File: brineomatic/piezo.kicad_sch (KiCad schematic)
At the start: 4 parts, among them Q2 AO3400A

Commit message: added qwiic i2c connector
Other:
- title: (none) -> https://github.com/hoeken/brineomatic
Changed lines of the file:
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@@
 	(generator_version "9.0")
 	(paper "A4")
+	(title_block
+		(title "https://github.com/hoeken/brineomatic")
+		(date "2025-08-28")
+		(rev "B")
+	)
 	(rectangle
 		(start 110.49 58.42)

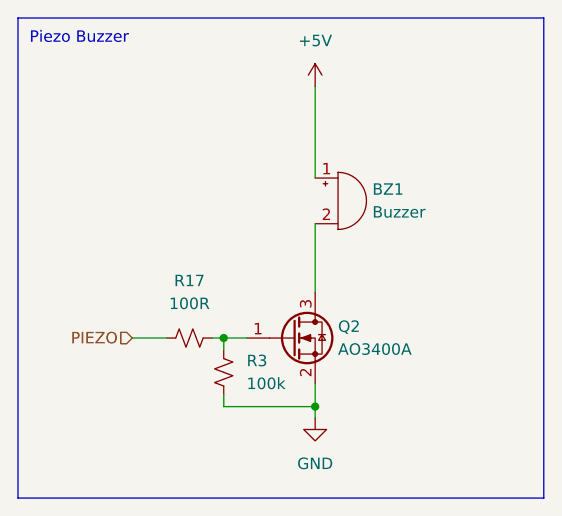
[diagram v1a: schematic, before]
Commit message: added pullup resistor to adc alert
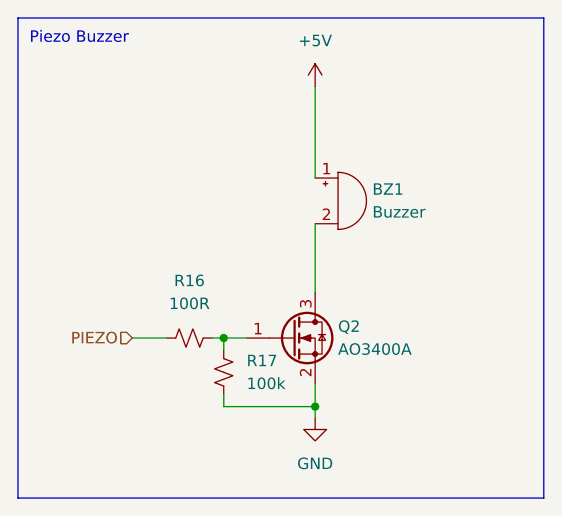
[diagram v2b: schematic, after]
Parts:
- renumbered R17 to R16, R3 to R17
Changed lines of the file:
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@@
 		(dnp no)
 		(fields_autoplaced yes)
-		(property "Reference" "#PWR023"
+		(property "Reference" "#PWR025"
 			(at 143.51 69.85 0)
 			(effects
@@
 			(project "brineomatic"
 				(path "/96477ae2-ef08-48f3-8dd4-fe4478541f68/d9651726-ebc8-4cdb-a521-a43a3039a77a"
-					(reference "#PWR023")
+					(reference "#PWR025")
 					(unit 1)
 				)
@@
 		(dnp no)
 		(fields_autoplaced yes)
-		(property "Reference" "R3"
+		(property "Reference" "R17"
 			(at 135.89 96.5199 0)
 			(effects
@@
 			(project "brineomatic"
 				(path "/96477ae2-ef08-48f3-8dd4-fe4478541f68/d9651726-ebc8-4cdb-a521-a43a3039a77a"
-					(reference "R3")
+					(reference "R17")
 					(unit 1)
 				)
@@
 		(dnp no)
 		(fields_autoplaced yes)
-		(property "Reference" "R17"
+		(property "Reference" "R16"
 			(at 129.54 87.63 90)
 			(effects
@@
 			(project "brineomatic"
 				(path "/96477ae2-ef08-48f3-8dd4-fe4478541f68/d9651726-ebc8-4cdb-a521-a43a3039a77a"
-					(reference "R17")
+					(reference "R16")
 					(unit 1)
 				)
@@
 		(dnp no)
 		(fields_autoplaced yes)
-		(property "Reference" "#PWR024"
+		(property "Reference" "#PWR026"
 			(at 143.51 109.22 0)
 			(effects
@@
 			(project "brineomatic"
 				(path "/96477ae2-ef08-48f3-8dd4-fe4478541f68/d9651726-ebc8-4cdb-a521-a43a3039a77a"
-					(reference "#PWR024")
-					(unit 1)
-				)
+					(reference "#PWR026")
+					(unit 1)
+				)

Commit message: added sendit piezo
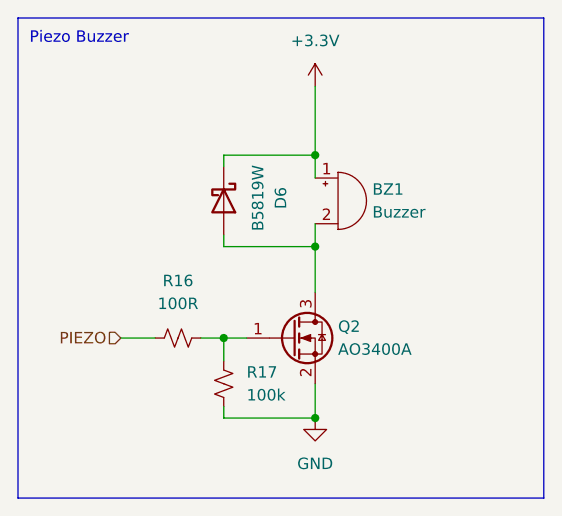
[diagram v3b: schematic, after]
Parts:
- added D6: B5819W, Diode_SMD:D_SOD-123, symbol Device:D_Schottky
- BZ1: footprint yarrboard:Buzzer_FUET_9.6x9.6 -> yarrboard:MagneticBuzzer_QMB-09B-03; LCSC C391033 -> C96256; Rotation Offset 90 -> (none)
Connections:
- net GND: now also R17.2; no longer R17.1
- net at Q2.1 (G), R16.1: now also R17.1; no longer R17.2
- net at BZ1.2 (-), Q2.3 (D): now also D6.2 (A)
- net +5V renamed +3.3V
- net +3.3V: now also D6.1 (K)
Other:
- title: https://github.com/hoeken/brineomatic -> https://github.com/hoeken/sendit
- moved on the sheet: R16

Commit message: added voltage divider to vref.  more component shuffling.
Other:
- title: https://github.com/hoeken/sendit -> https://github.com/hoeken/brineomatic
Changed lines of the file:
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@@
 	(paper "A4")
 	(title_block
-		(title "https://github.com/hoeken/sendit")
+		(title "https://github.com/hoeken/brineomatic")
 		(date "2025-08-28")
 		(rev "C")

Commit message: power routing is done.
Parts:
- R17: value 100k -> 10k
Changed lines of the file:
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@@
 			)
 		)
-		(property "Value" "100k"
+		(property "Value" "10k"
 			(at 135.89 100.3299 0)
 			(effects

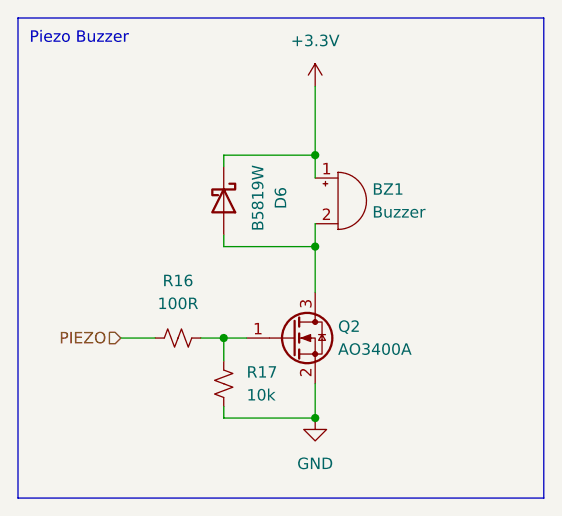
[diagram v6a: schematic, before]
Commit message: more esd protection, drc passing, silkscreen fixed
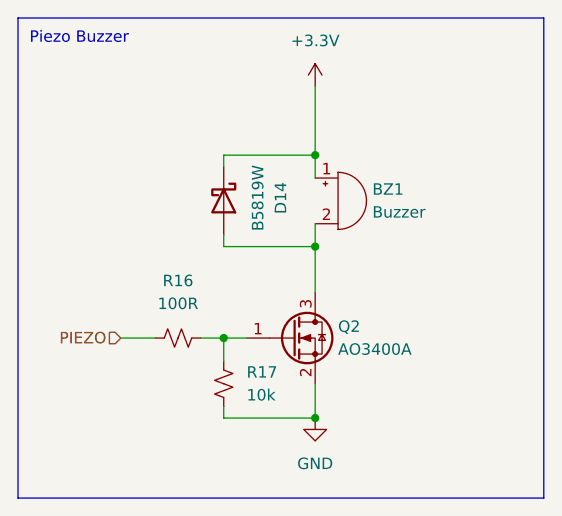
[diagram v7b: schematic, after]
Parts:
- renumbered D6 to D14
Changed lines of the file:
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@@
 		(on_board yes)
 		(dnp no)
-		(property "Reference" "D6"
+		(property "Reference" "D14"
 			(at 139.7 78.4225 0)
 			(effects
@@
 			(project "brineomatic"
 				(path "/96477ae2-ef08-48f3-8dd4-fe4478541f68/d9651726-ebc8-4cdb-a521-a43a3039a77a"
-					(reference "D6")
+					(reference "D14")
 					(unit 1)
 				)

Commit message: value and component updates
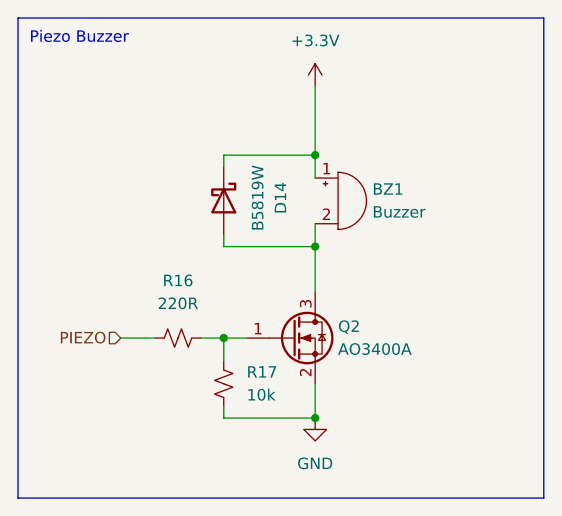
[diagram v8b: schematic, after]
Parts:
- R16: value 100R -> 220R
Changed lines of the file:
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@@
 			)
 		)
-		(property "Value" "100R"
+		(property "Value" "220R"
 			(at 128.27 90.17 90)
 			(effects
